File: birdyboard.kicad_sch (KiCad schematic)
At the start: 41 parts, among them J1 24V Input Screw Terminal, J12 AS5047_Adapter_Board_Connector, J13 AS5047_Adapter_Board_Connector, J14 AS5047_Adapter_Board_Connector, J15 AS5047_Adapter_Board_Connector, J2 24V Input Screw Terminal, J3 24V Input Screw Terminal, J5 JST-PH StepMotor Conn, J9 TBP02R2-381-04BE, U0 Pico, U1 TMC2209_SILENTSTEPSTICK, U2 TMC2209_SILENTSTEPSTICK, U3 TMC2209_SILENTSTEPSTICK, U4 TMC2209_SILENTSTEPSTICK, U5 K7805-3AR3, U6 AZ1117CH-3_3TRG1, U6 SN74CBT3253 MUX/DEMUX

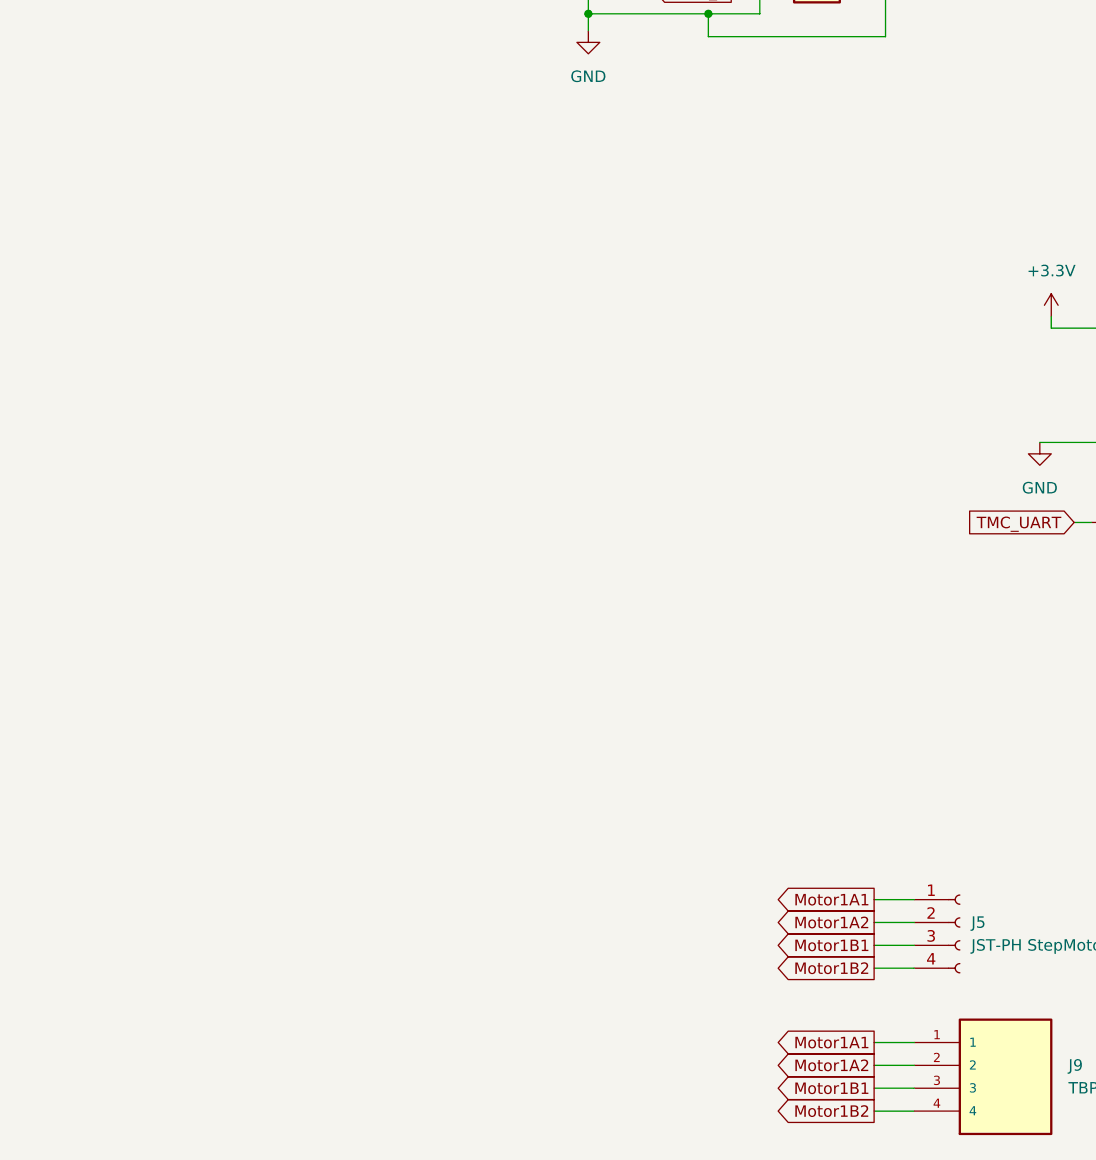
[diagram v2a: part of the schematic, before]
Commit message: Adds 7 sensor inputs for limit switches and what not
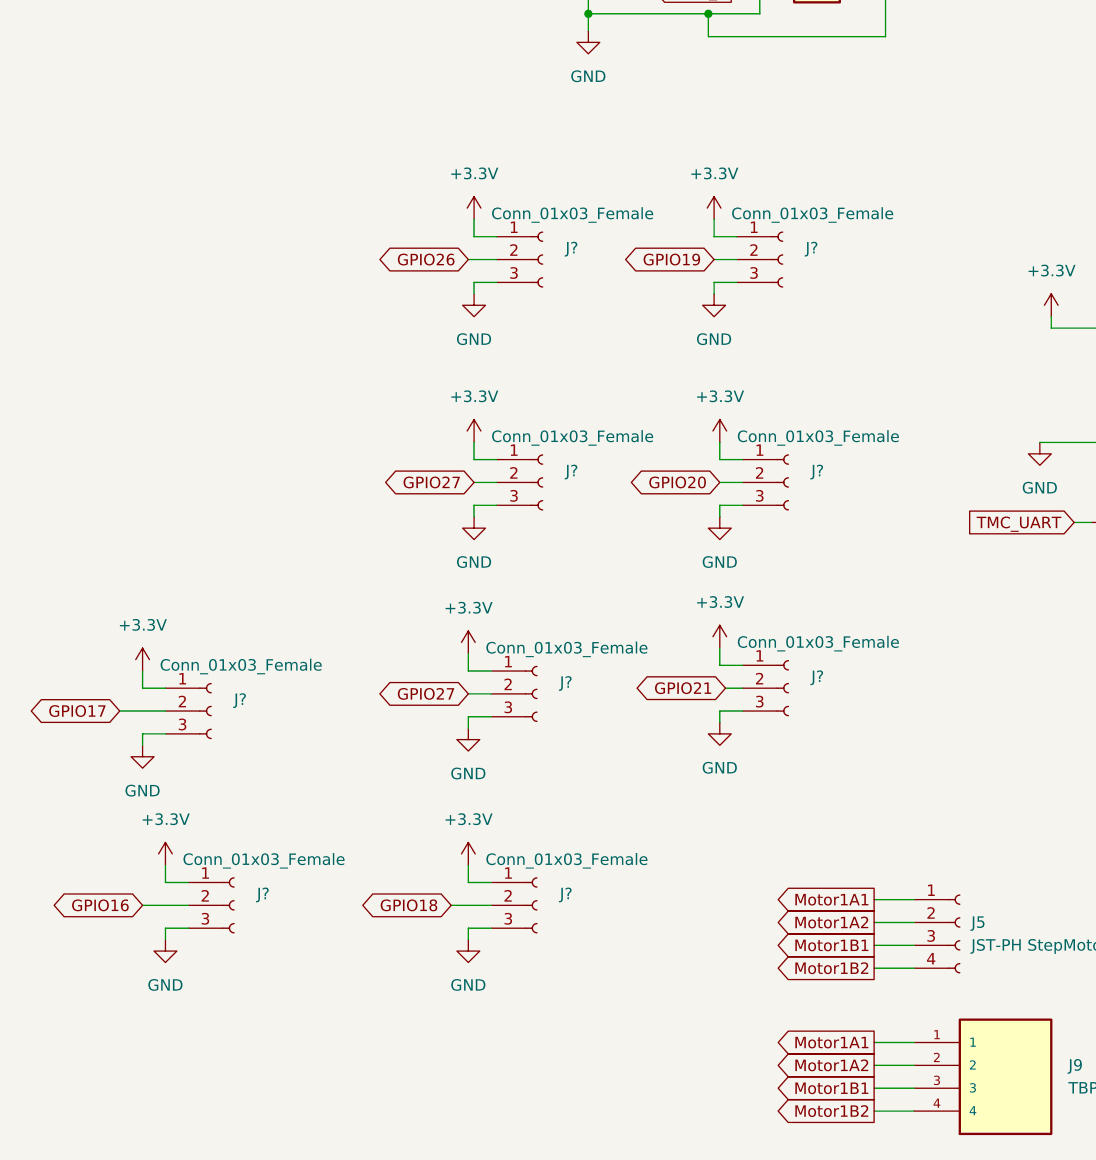
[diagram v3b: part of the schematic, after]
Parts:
- added J? (x9): Conn_01x03_Female, symbol Connector:Conn_01x03_Female
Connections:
- net +3V3: now also J?.1 (Pin_1), J?.1 (Pin_1), J?.1 (Pin_1), J?.1 (Pin_1), J?.1 (Pin_1), J?.1 (Pin_1), J?.1 (Pin_1), J?.1 (Pin_1), J?.1 (Pin_1)
- net GND: now also J?.3 (Pin_3), J?.3 (Pin_3), J?.3 (Pin_3), J?.3 (Pin_3), J?.3 (Pin_3), J?.3 (Pin_3), J?.3 (Pin_3), J?.3 (Pin_3), J?.3 (Pin_3)
- net GPIO16: now also J?.2 (Pin_2)
- net GPIO17: now also J?.2 (Pin_2)
- net GPIO18: now also J?.2 (Pin_2)
- net GPIO19: now also J?.2 (Pin_2)
- net GPIO20: now also J?.2 (Pin_2)
- net GPIO21: now also J?.2 (Pin_2)
- net GPIO26: now also J?.2 (Pin_2)
- net GPIO27: now also J?.2 (Pin_2), J?.2 (Pin_2)

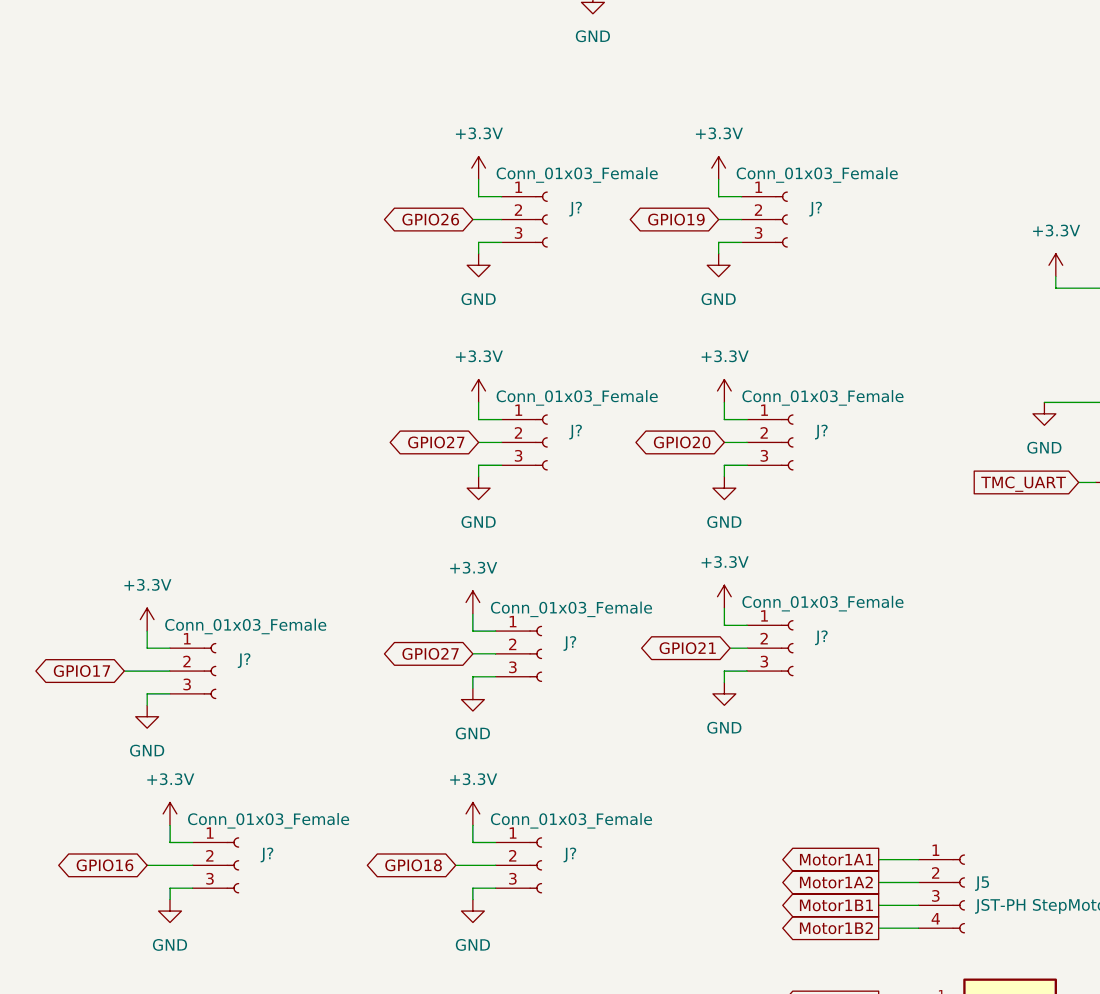
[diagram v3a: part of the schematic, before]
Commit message: Adds pull ups to 3 sensor inputs, just for good measure
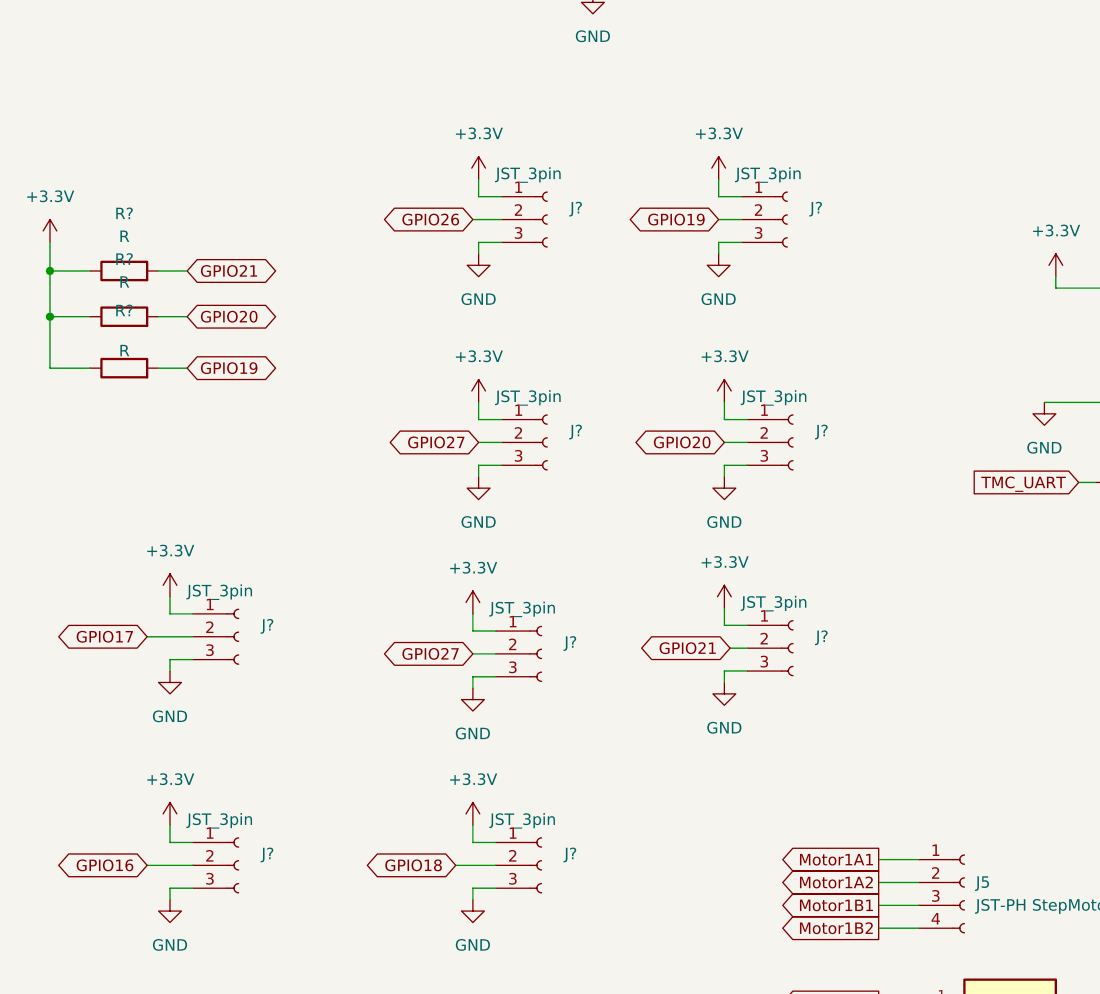
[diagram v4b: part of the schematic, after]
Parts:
- removed J? (x8): Conn_01x03_Female, symbol Connector:Conn_01x03_Female
- added J? (x8): JST_3pin, Connector_JST:JST_XH_B3B-XH-A_1x03_P2.50mm_Vertical, symbol Connector:Conn_01x03_Female
- added R? (x3): R, symbol Device:R
- J?: value Conn_01x03_Female -> JST_3pin; footprint (none) -> Connector_JST:JST_XH_B3B-XH-A_1x03_P2.50mm_Vertical
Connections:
- net +3V3: now also J?.1 (Pin_1), J?.1 (Pin_1), J?.1 (Pin_1), J?.1 (Pin_1), J?.1 (Pin_1), J?.1 (Pin_1), J?.1 (Pin_1), J?.1 (Pin_1), R?.1, R?.1, R?.1
- net GND: now also J?.3 (Pin_3), J?.3 (Pin_3), J?.3 (Pin_3), J?.3 (Pin_3), J?.3 (Pin_3), J?.3 (Pin_3), J?.3 (Pin_3), J?.3 (Pin_3)
- net GPIO16: now also J?.2 (Pin_2)
- net GPIO17: now also J?.2 (Pin_2)
- net GPIO18: now also J?.2 (Pin_2)
- net GPIO19: now also J?.2 (Pin_2), R?.2
- net GPIO20: now also J?.2 (Pin_2), R?.2
- net GPIO21: now also J?.2 (Pin_2), R?.2
- net GPIO27: now also J?.2 (Pin_2), J?.2 (Pin_2)

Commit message: Fixes most footprints and places footprints roughly at their final resting place
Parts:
- removed J1, J2, J3: 24V Input Screw Terminal, birdyboard:CUI_TBP01R2-508-02BE, symbol Connector:Screw_Terminal_01x02
- removed J?: JST_3pin, Connector_JST:JST_XH_B3B-XH-A_1x03_P2.50mm_Vertical, symbol Connector:Conn_01x03_Female
- added J13, J14, J15: Screw_Terminal_01x02, birdyboard:CUI_TBP01R2-508-02BE, symbol Connector:Screw_Terminal_01x02
- C1: footprint (none) -> Capacitor_SMD:C_0805_2012Metric_Pad1.18x1.45mm_HandSolder
- C2: renamed from C3; footprint (none) -> Capacitor_SMD:C_0805_2012Metric_Pad1.18x1.45mm_HandSolder
- C3: renamed from C4; footprint (none) -> Capacitor_SMD:C_0805_2012Metric_Pad1.18x1.45mm_HandSolder
- C4: renamed from C2; footprint (none) -> Capacitor_SMD:C_0805_2012Metric_Pad1.18x1.45mm_HandSolder
- J10: renamed from J?; footprint Connector_PinHeader_2.54mm:PinHeader_2x20_P2.54mm_Vertical -> Connector_PinHeader_2.54mm:PinHeader_2x20_P2.54mm_Vertical_SMD
- J21: renamed from J?; value JST-PH StepMotor Conn -> JST-PH UART Conn
- J24: renamed from J12; footprint (none) -> Connector_PinHeader_2.54mm:PinHeader_2x08_P2.54mm_Vertical_SMD
- J25: renamed from J13; footprint (none) -> Connector_PinHeader_2.54mm:PinHeader_2x08_P2.54mm_Vertical_SMD
- J26: renamed from J14; footprint (none) -> Connector_PinHeader_2.54mm:PinHeader_2x08_P2.54mm_Vertical_SMD
- J27: renamed from J15; footprint (none) -> Connector_PinHeader_2.54mm:PinHeader_2x08_P2.54mm_Vertical_SMD
- JP1, JP2, JP3, JP4: renamed from JP?; footprint (none) -> Jumper:SolderJumper-3_P1.3mm_Bridged2Bar12_Pad1.0x1.5mm_NumberLabels
- JP5: renamed from JP1; footprint (none) -> Jumper:SolderJumper-3_P1.3mm_Bridged2Bar12_Pad1.0x1.5mm_NumberLabels
- JP6: renamed from JP?; footprint (none) -> Connector_PinHeader_2.54mm:PinHeader_1x02_P2.54mm_Vertical
- R1, R2, R3, R4, R5, R6, R7, R8: renamed from R?; footprint (none) -> Resistor_SMD:R_0805_2012Metric_Pad1.20x1.40mm_HandSolder
- U1: footprint MODULE_TMC2208_SILENTSTEPSTICK -> birdyboard:TMC2208_SILENTSTEPSTICK
- U2: renamed from U3; footprint MODULE_TMC2208_SILENTSTEPSTICK -> birdyboard:TMC2208_SILENTSTEPSTICK
- U4: renamed from U2; footprint MODULE_TMC2208_SILENTSTEPSTICK -> birdyboard:TMC2208_SILENTSTEPSTICK
- U5: renamed from U4; footprint MODULE_TMC2208_SILENTSTEPSTICK -> birdyboard:TMC2208_SILENTSTEPSTICK
- U6: footprint (none) -> Package_SO:TSSOP-16_4.4x5mm_P0.65mm
- gave numbers to parts that had none: 15
- renumbered J5 to J11, J9 to J12, U0 to U3, U6 to U7, U5 to U8
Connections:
- net +24V: now also J13.1 (Pin_1), J14.1 (Pin_1)
- net +3V3: now also U1.JP2_7 (VIO), U4.JP2_7 (VIO)
- net +5V: now also J15.1 (Pin_1)
- net GND: now also J13.2 (Pin_2), J14.2 (Pin_2), J15.2 (Pin_2)
